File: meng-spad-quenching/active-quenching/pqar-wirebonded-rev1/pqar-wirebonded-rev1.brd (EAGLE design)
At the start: 46 x 46 mm, 62 parts, among them IC1 SPAD, IC2 NL17SZ125, IC3 74AUC1G32DCK, IC4 BCV62, IC5 NC7SV74K8X, IC6 74AHC1G14DCK, IC7 74LVC1G02DCK, IC8 LTC1711, IC9 NC7WZ16P6X, U1 SN74LVC1G123DCUT, X1 I_HOLDOFF, X2 V_LOGIC, X3 FORCE_QUENCH, X4 OUT, X5 V_A

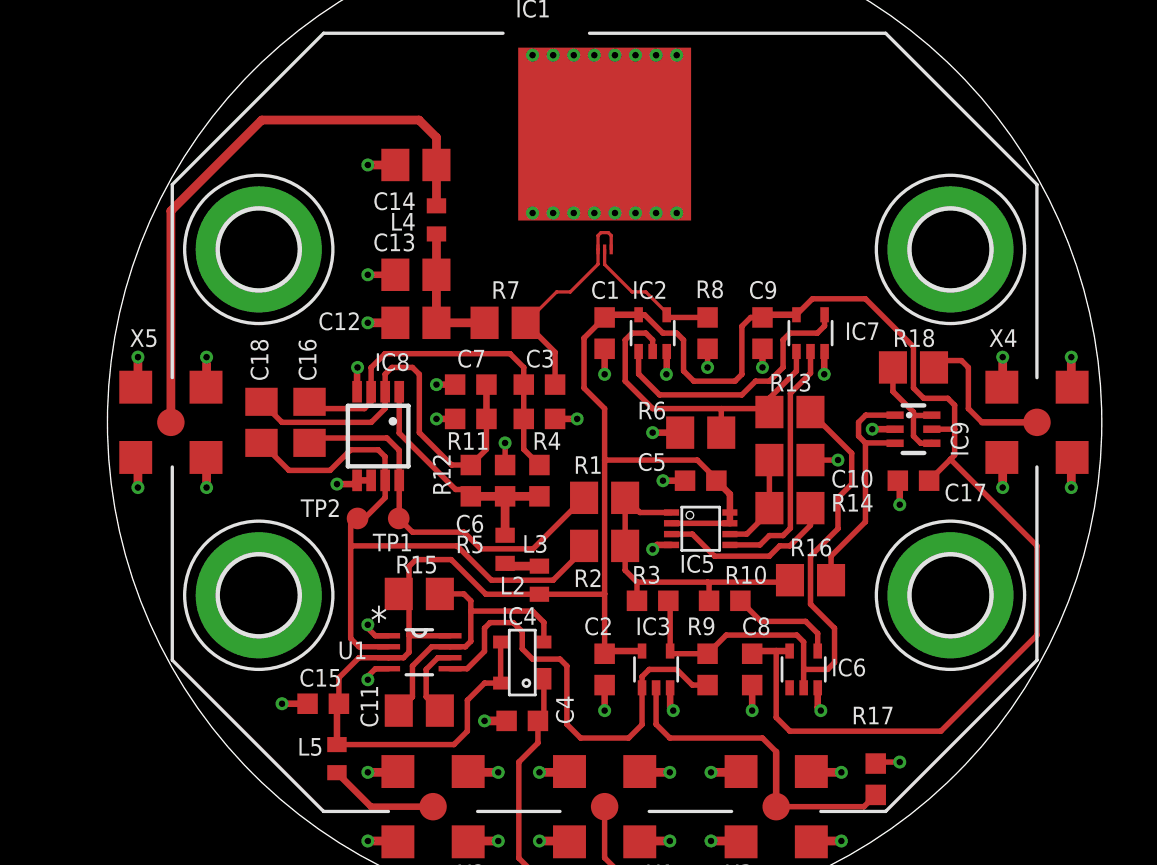
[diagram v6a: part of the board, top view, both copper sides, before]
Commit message: Add wirebonding pads for substrate bias
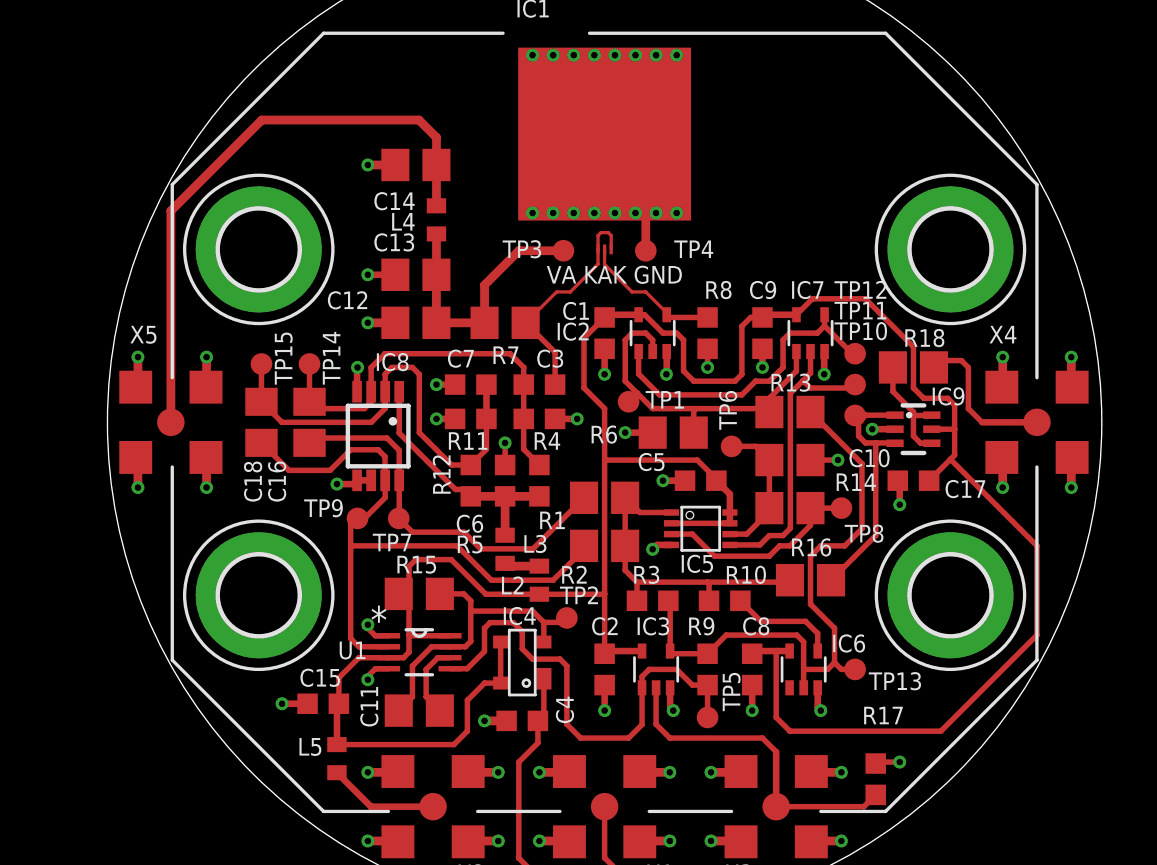
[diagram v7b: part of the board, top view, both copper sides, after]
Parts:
- added TP10, TP11, TP12, TP13, TP14, TP15, TP3, TP4, TP5, TP6, TP7, TP8, TP9: AV_DET, testpad:TP10R
- moved TP1 11.9 mm to (1.11, 0.95)
- moved TP2 10.7 mm to (-1.75, -9.05)
- moved R6 1.27 mm to (3.17, -0.48)
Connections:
- net !AV_DET: now also TP7.TP; no longer TP1.TP
- net !EN_DRIVER: now also TP12.TP
- net !RESET: now also TP8.TP
- net !RESET_RC: now also TP6.TP
- net AV_DET: now also TP9.TP; no longer TP2.TP
- net AV_DET_REF: now also TP15.TP
- net CLK_RESET_JUMP: now also TP10.TP
- net DRIVER_IN: now also TP1.TP
- net GND: now also TP4.TP
- net HOLDOFF_CAP: now also TP2.TP
- net HOLDOFF_TIMER: now also TP5.TP
- net KATHODE_C: now also TP14.TP
- net QUENCH: now also TP13.TP
- net RESET: now also TP11.TP
- net V_A_FILT: now also TP3.TP
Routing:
- net GND: track 65.8 -> 72.0 mm
- net V_A_FILT: track 6.34 -> 12.4 mm
- net RESET: track 11.7 -> 14.3 mm
- net QUENCH: track 26.4 -> 28.5 mm
- net !RESET_RC: track 4.64 -> 6.65 mm
- net !EN_DRIVER: track 12.6 -> 14.6 mm
- net KATHODE_C: track 17.1 -> 18.8 mm
- net AV_DET_REF: track 19.5 -> 21.3 mm
- net HOLDOFF_TIMER: track 20.6 -> 22.1 mm
- net !RESET: track 8.24 -> 9.67 mm
- net HOLDOFF_CAP: track 13.4 -> 14.6 mm
- net DRIVER_IN: track 15.7 -> 16.2 mm
- net CLK_RESET_JUMP: track 11.3 -> 11.8 mm
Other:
- board text added: "VA KAK GND"

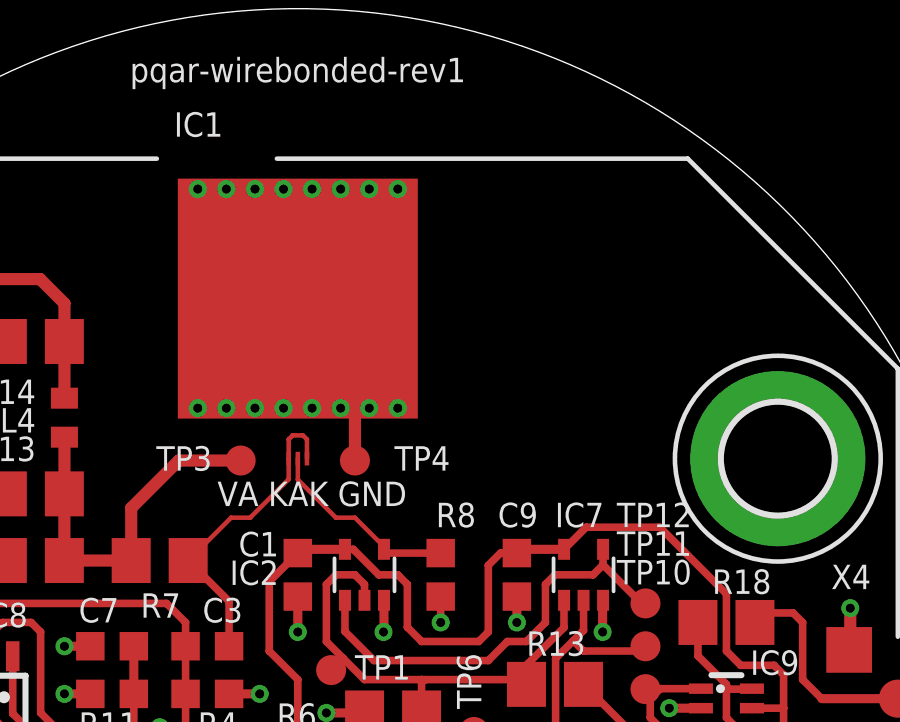
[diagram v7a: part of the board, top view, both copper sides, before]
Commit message: Created BOM
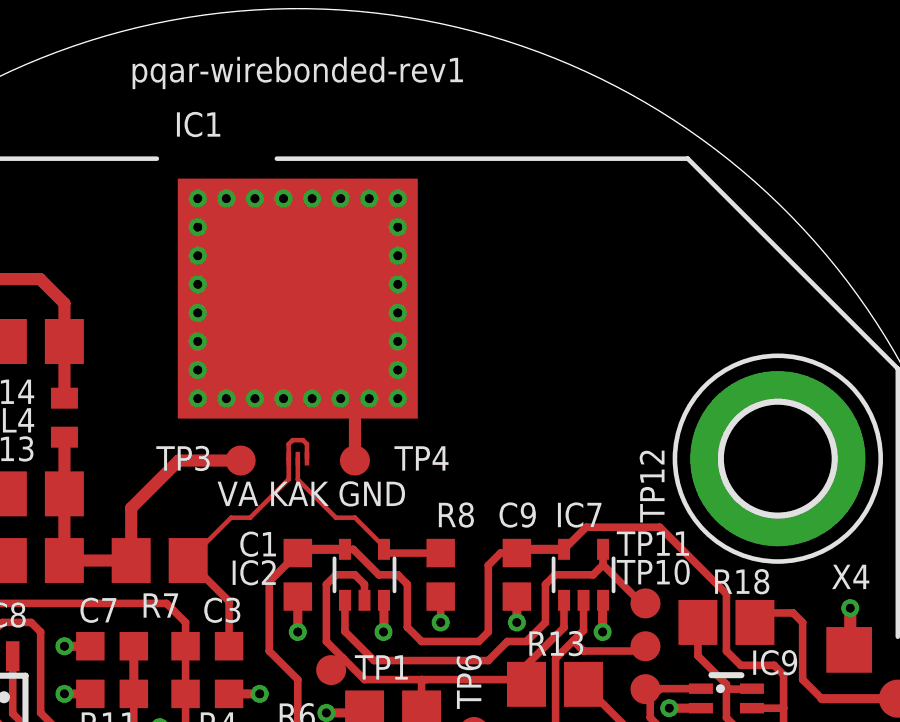
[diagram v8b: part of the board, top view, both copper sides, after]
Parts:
- C1, C15, C8, C9: value IPDiA 935131425610 -> CAP CER 0.1UF 50V X7R 0603 5%
- C11: value CAP CER 0.1UF 50V X7R 0805 5% -> CAP FILM 100PF 5% 0805
- C7: value CAP CER 0.1UF 50V X7R 0603 5% -> DNP
- IC2: value NL17SZ125 -> NL17SZ125DFT2G
- IC3: value 74AUC1G32DCK -> NL17SZ32DFT2G
- IC6: value 74AHC1G14DCK -> NL17SZ14DFT2G
- IC7: value 74LVC1G02DCK -> NL17SZ02DFT2G
- IC8: value LTC1711 -> LT1711
- L1, L2, L3, L4, L5: value Samsung CIM05J152NC -> FERRITE BEAD 1.5 KOHM 0402 1LN
- R11, R5: value RES SMD 1K OHM 1% 1/10W 0603 -> RES SMD 10.2K OHM 1% 1/10W 0603
- R12, R4: value RES SMD 1K OHM 1% 1/10W 0603 -> RES SMD 10K OHM 1% 1/10W 0603
- R18: value RES SMD 49.9 OHM 1% 1/10W 0805 -> RES SMD 49.9 OHM 1% 1/8W 0805
- R8: value RES SMD 10M OHM 1% 1/10W 0603 -> RES SMD 10M OHM 5% 1/10W 0603
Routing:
- net GND: track 72.0 -> 71.7 mm, vias 65 -> 77
